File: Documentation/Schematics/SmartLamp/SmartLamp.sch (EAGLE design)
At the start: 25 parts, among them IC1 DS3231/SO, J1 POWER_JACKPTH_BREAD, Q1 IRF1404, Q2 IRF1404, Q3 IRF1404, U1 HM-10

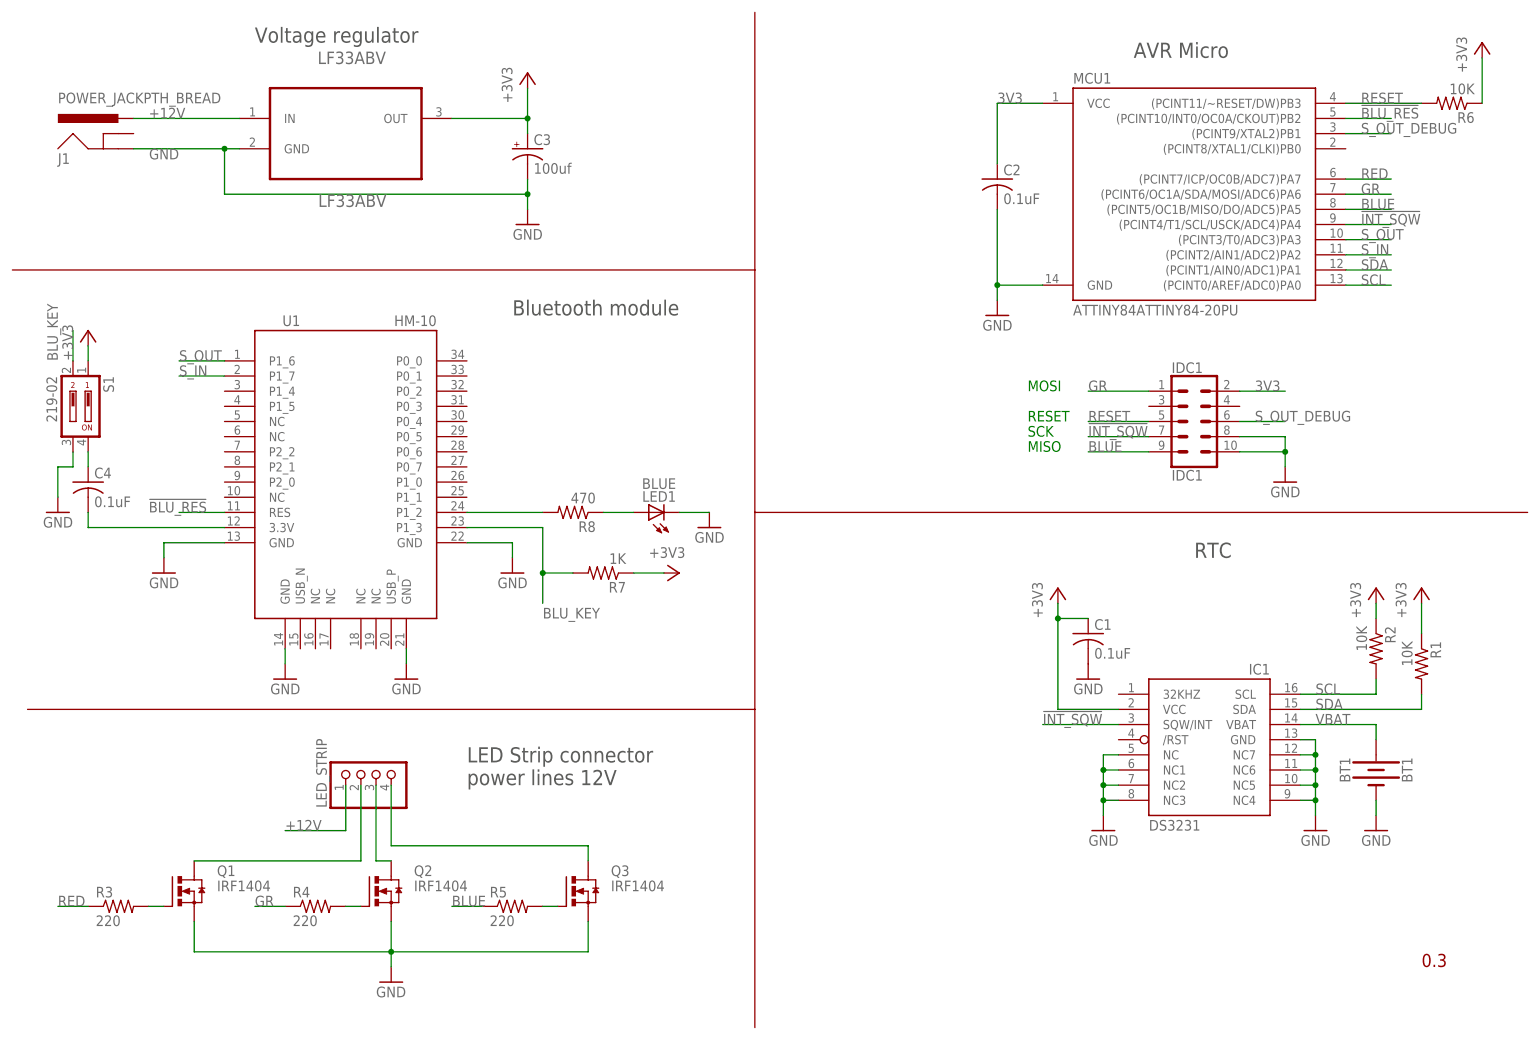
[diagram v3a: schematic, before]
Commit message: Replaced RTC device, battery holder and switch, parts to buy..
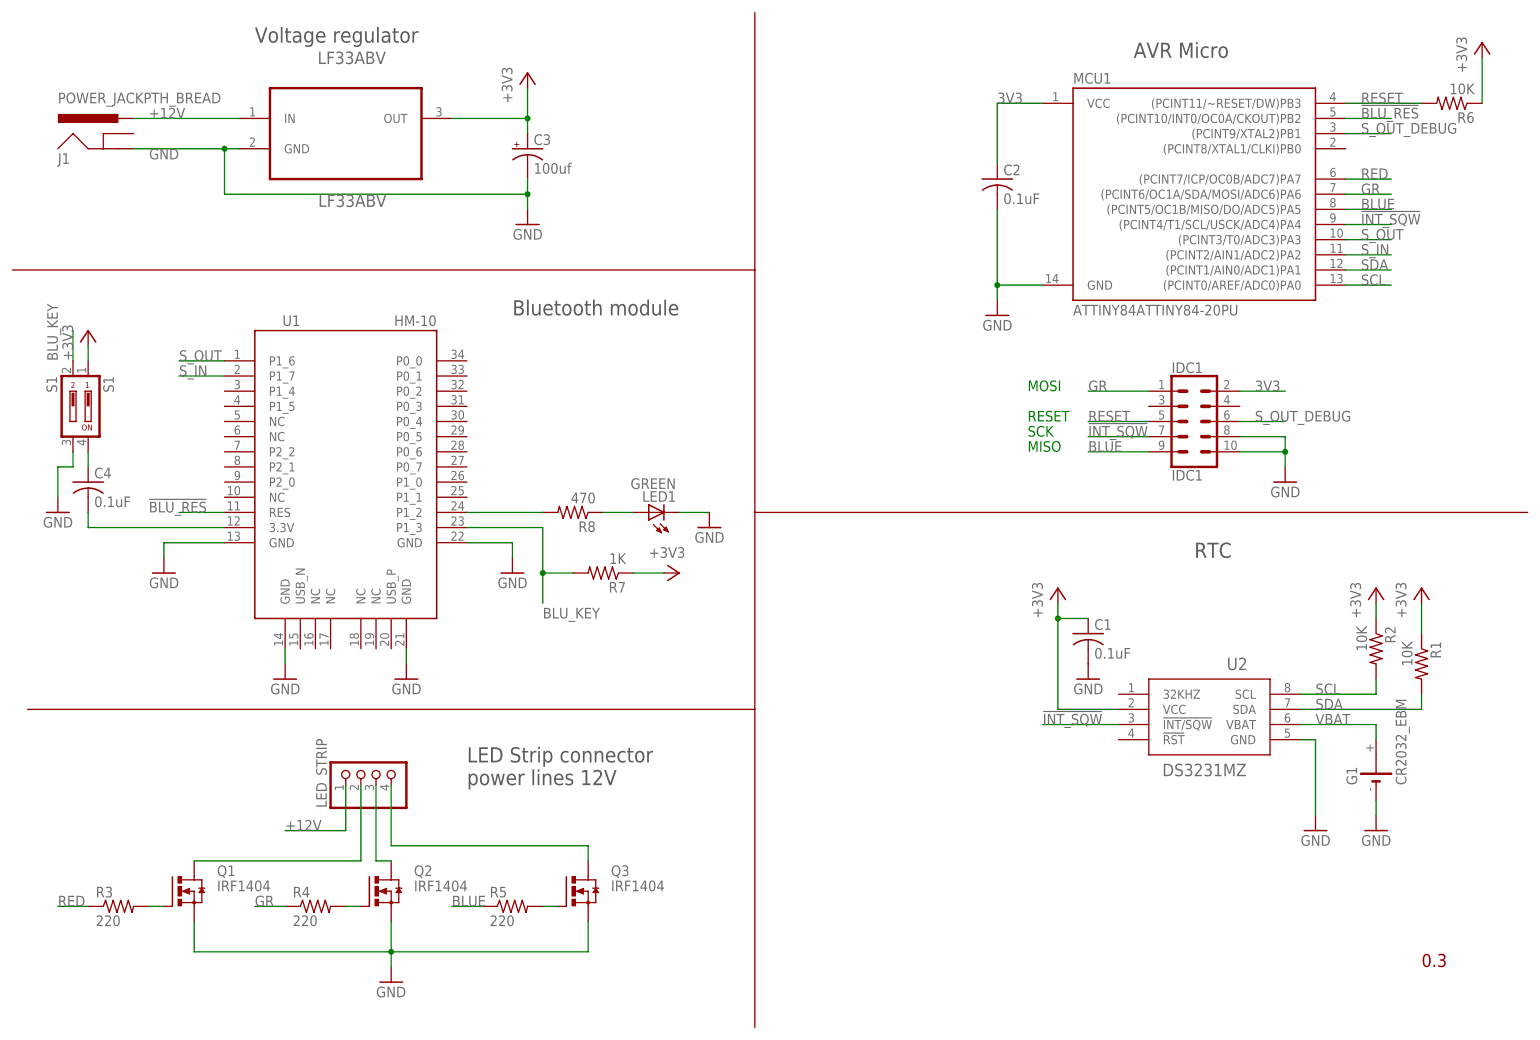
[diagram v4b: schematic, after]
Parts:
- removed BT1: BT1, SparkFun-Batteries:BATTERY-20MM_SMD_4LEGS
- removed IC1: DS3231/SO, adafruit:DS3231/SO
- added G1: CR2032_EBM, CuSTOM_GB:CR2032_EBM
- added U2: DS3231MZ, Maxim_RTC:DS3231MZ
- LED1: value BLUE -> GREEN
- S1: value 219-02 -> S1; device switch-dil:219-02 -> switch-dil:SD4-02
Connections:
- net !INT_SQW: now also U2.!INT/SQW; no longer IC1.SQW/INT
- net +3V3: now also U2.VCC; no longer IC1.VCC
- net GND: now also G1.-, U2.GND; no longer BT1.-, IC1.GND, IC1.NC, IC1.NC1, IC1.NC2, IC1.NC3, IC1.NC4, IC1.NC5, IC1.NC6, IC1.NC7
- net SCL: now also U2.SCL; no longer IC1.SCL
- net SDA: now also U2.SDA; no longer IC1.SDA
- net VBAT: now also G1.+, U2.VBAT; no longer BT1.+, IC1.VBAT

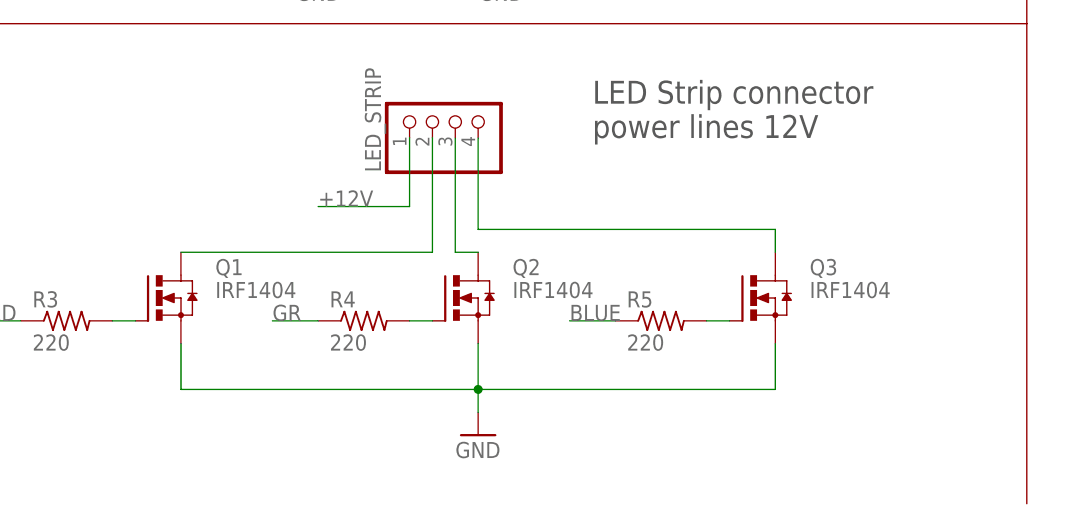
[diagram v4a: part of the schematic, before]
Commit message: Added datasheet for new mosfet IRLZ44n, small changes to HM-10 test program.
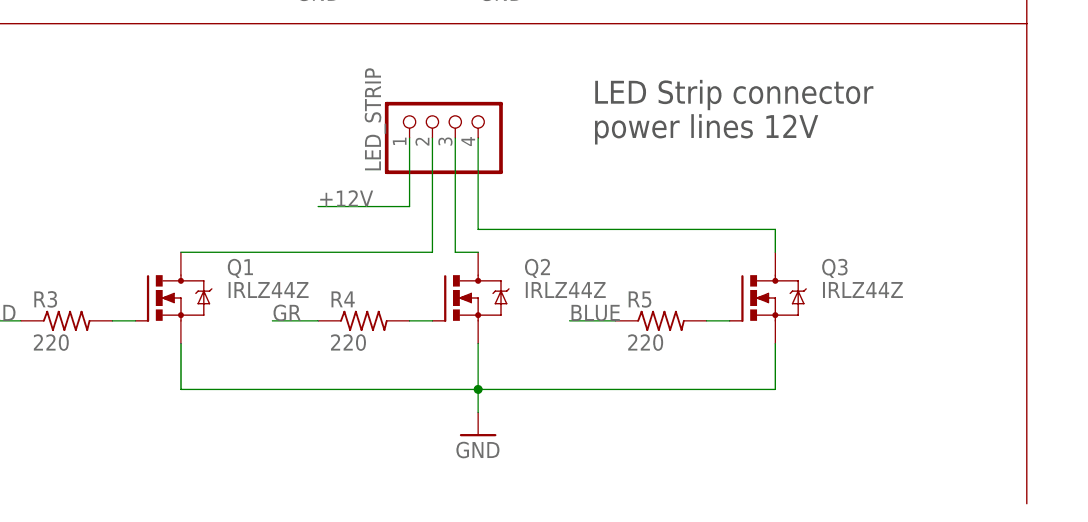
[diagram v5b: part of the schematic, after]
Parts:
- Q1, Q2, Q3: value IRF1404 -> IRLZ44Z; device transistor-power:IRFI540NPBF -> transistor-power:IRLZ44Z
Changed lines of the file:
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@@
 <part name="GND12" library="supply1" deviceset="GND" device=""/>
 <part name="C4" library="adafruit" deviceset="C-US" device="025-024X044" value="0.1uF"/>
-<part name="Q1" library="transistor-power" deviceset="IRFI540NPBF" device="" value="IRF1404"/>
-<part name="Q2" library="transistor-power" deviceset="IRFI540NPBF" device="" value="IRF1404"/>
-<part name="Q3" library="transistor-power" deviceset="IRFI540NPBF" device="" value="IRF1404"/>
 <part name="GND10" library="supply1" deviceset="GND" device=""/>
 <part name="LED_STRIP" library="pinhead" deviceset="PINHD-1X4" device=""/>
@@
 <part name="G1" library="CuSTOM_GB" deviceset="CR2032_EBM" device=""/>
 <part name="U2" library="Maxim_RTC" deviceset="DS3231MZ" device=""/>
+<part name="Q1" library="transistor-power" deviceset="IRLZ44Z" device=""/>
+<part name="Q2" library="transistor-power" deviceset="IRLZ44Z" device=""/>
+<part name="Q3" library="transistor-power" deviceset="IRLZ44Z" device=""/>
 </parts>
 <sheets>
@@
 <instance part="GND12" gate="1" x="119.38" y="88.9" rot="MR0"/>
 <instance part="C4" gate="G$1" x="15.24" y="96.52"/>
-<instance part="Q1" gate="G$1" x="30.48" y="27.94"/>
-<instance part="Q2" gate="G$1" x="63.5" y="27.94"/>
-<instance part="Q3" gate="G$1" x="96.52" y="27.94"/>
 <instance part="GND10" gate="1" x="66.04" y="12.7"/>
 <instance part="LED_STRIP" gate="A" x="63.5" y="48.26" rot="R90"/>
@@
 <instance part="G1" gate="G$1" x="231.14" y="48.26" rot="R90"/>
 <instance part="U2" gate="A" x="203.2" y="58.42"/>
+<instance part="Q1" gate="G$1" x="30.48" y="27.94"/>
+<instance part="Q2" gate="G$1" x="63.5" y="27.94"/>
+<instance part="Q3" gate="G$1" x="96.52" y="27.94"/>
 </instances>
 <busses>
@@
 </segment>
 <segment>
-<pinref part="Q1" gate="G$1" pin="S"/>
 <wire x1="33.02" y1="22.86" x2="33.02" y2="17.78" width="0.1524" layer="91"/>
-<pinref part="Q2" gate="G$1" pin="S"/>
 <wire x1="33.02" y1="17.78" x2="66.04" y2="17.78" width="0.1524" layer="91"/>
 <wire x1="66.04" y1="17.78" x2="66.04" y2="22.86" width="0.1524" layer="91"/>
-<pinref part="Q3" gate="G$1" pin="S"/>
 <wire x1="99.06" y1="22.86" x2="99.06" y2="17.78" width="0.1524" layer="91"/>
 <wire x1="99.06" y1="17.78" x2="66.04" y2="17.78" width="0.1524" layer="91"/>
@@
 <pinref part="GND10" gate="1" pin="GND"/>
 <wire x1="66.04" y1="15.24" x2="66.04" y2="17.78" width="0.1524" layer="91"/>
+<pinref part="Q1" gate="G$1" pin="S"/>
+<pinref part="Q2" gate="G$1" pin="S"/>
+<pinref part="Q3" gate="G$1" pin="S"/>
 </segment>
 <segment>
@@
 <net name="N$3" class="1">
 <segment>
-<pinref part="Q1" gate="G$1" pin="D"/>
 <wire x1="33.02" y1="33.02" x2="60.96" y2="33.02" width="0.1524" layer="91"/>
 <pinref part="LED_STRIP" gate="A" pin="2"/>
 <wire x1="60.96" y1="45.72" x2="60.96" y2="33.02" width="0.1524" layer="91"/>
+<pinref part="Q1" gate="G$1" pin="D"/>
 </segment>
 </net>
 <net name="N$4" class="1">
 <segment>
-<pinref part="Q2" gate="G$1" pin="D"/>
 <wire x1="63.5" y1="33.02" x2="66.04" y2="33.02" width="0.1524" layer="91"/>
 <pinref part="LED_STRIP" gate="A" pin="3"/>
 <wire x1="63.5" y1="33.02" x2="63.5" y2="45.72" width="0.1524" layer="91"/>
+<pinref part="Q2" gate="G$1" pin="D"/>
 </segment>
 </net>
 <net name="N$6" class="1">
 <segment>
-<pinref part="Q3" gate="G$1" pin="D"/>
 <wire x1="66.04" y1="35.56" x2="99.06" y2="35.56" width="0.1524" layer="91"/>
 <wire x1="99.06" y1="35.56" x2="99.06" y2="33.02" width="0.1524" layer="91"/>
 <pinref part="LED_STRIP" gate="A" pin="4"/>
 <wire x1="66.04" y1="45.72" x2="66.04" y2="35.56" width="0.1524" layer="91"/>
+<pinref part="Q3" gate="G$1" pin="D"/>
 </segment>
 </net>
 <net name="N$7" class="0">
 <segment>
-<pinref part="Q1" gate="G$1" pin="G"/>
 <pinref part="R3" gate="G$1" pin="2"/>
 <wire x1="27.94" y1="25.4" x2="25.4" y2="25.4" width="0.1524" layer="91"/>
+<pinref part="Q1" gate="G$1" pin="G"/>
 </segment>
 </net>
@@
 <segment>
 <pinref part="R4" gate="G$1" pin="2"/>
+<wire x1="58.42" y1="25.4" x2="60.96" y2="25.4" width="0.1524" layer="91"/>
 <pinref part="Q2" gate="G$1" pin="G"/>
-<wire x1="58.42" y1="25.4" x2="60.96" y2="25.4" width="0.1524" layer="91"/>
 </segment>
 </net>
@@
 <segment>
 <pinref part="R5" gate="G$1" pin="2"/>
+<wire x1="91.44" y1="25.4" x2="93.98" y2="25.4" width="0.1524" layer="91"/>
 <pinref part="Q3" gate="G$1" pin="G"/>
-<wire x1="91.44" y1="25.4" x2="93.98" y2="25.4" width="0.1524" layer="91"/>
-</segment>
-</net>
+</segment>
+</net>

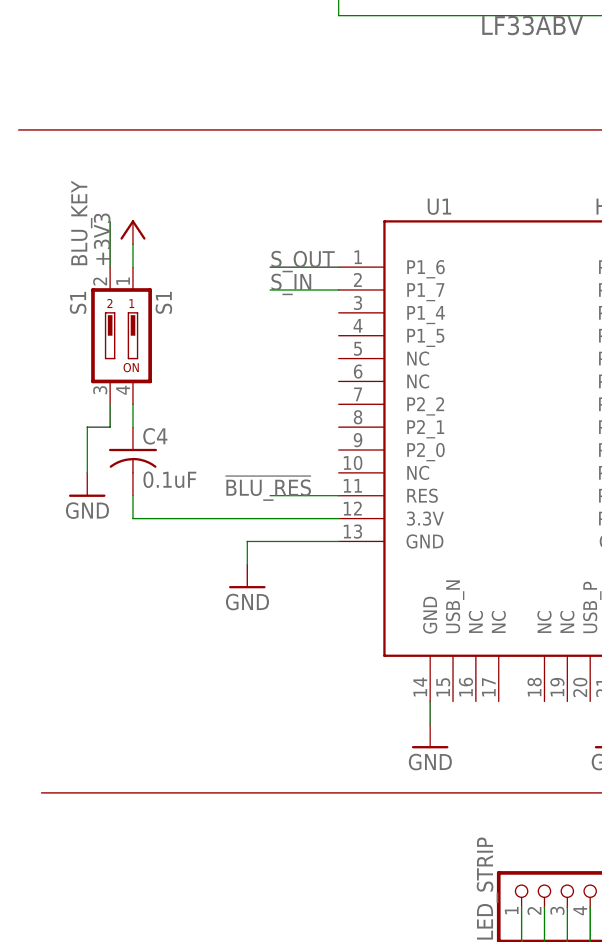
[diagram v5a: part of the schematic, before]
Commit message: Changed dip switch to cut GND instead of VCC to bluetooth module.
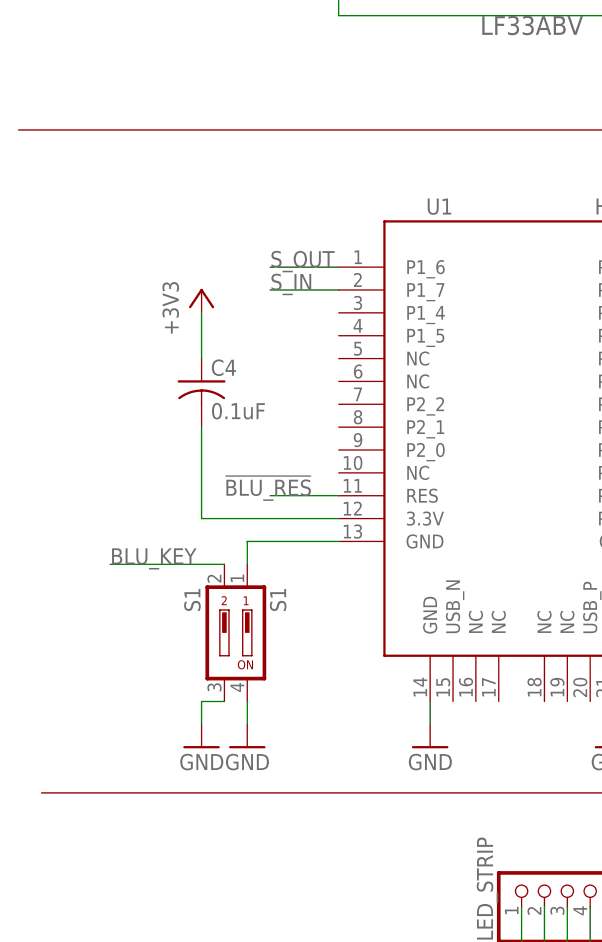
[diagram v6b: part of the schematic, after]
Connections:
- net +3V3: now also C4.1; no longer S1.1
- net GND: now also S1.4; no longer U1.GND@1
- net N$1: no longer C4.2
- net N$2: now also S1.1, U1.GND@1; no longer C4.1, S1.4
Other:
- moved on the sheet: C4, S1
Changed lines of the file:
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@@
 <instance part="R8" gate="G$1" x="96.52" y="91.44" rot="R180"/>
 <instance part="LED1" gate="G$1" x="109.22" y="91.44" rot="R90"/>
-<instance part="GND7" gate="1" x="27.94" y="81.28" rot="MR0"/>
+<instance part="GND7" gate="1" x="27.94" y="63.5" rot="MR0"/>
 <instance part="GND8" gate="1" x="48.26" y="63.5" rot="MR0"/>
 <instance part="GND9" gate="1" x="68.58" y="63.5" rot="MR0"/>
 <instance part="GND11" gate="1" x="86.36" y="81.28" rot="MR0"/>
 <instance part="GND12" gate="1" x="119.38" y="88.9" rot="MR0"/>
-<instance part="C4" gate="G$1" x="15.24" y="96.52"/>
+<instance part="C4" gate="G$1" x="22.86" y="104.14"/>
 <instance part="GND10" gate="1" x="66.04" y="12.7"/>
 <instance part="LED_STRIP" gate="A" x="63.5" y="48.26" rot="R90"/>
@@
 <instance part="FRAME1" gate="G$1" x="0" y="0"/>
 <instance part="GND13" gate="1" x="231.14" y="38.1" rot="MR0"/>
-<instance part="S1" gate="1" x="15.24" y="109.22" rot="R180"/>
+<instance part="S1" gate="1" x="27.94" y="76.2" rot="R180"/>
 <instance part="+3V1" gate="G$1" x="248.92" y="170.18"/>
 <instance part="+3V2" gate="G$1" x="177.8" y="78.74"/>
@@
 <instance part="+3V5" gate="G$1" x="88.9" y="165.1"/>
 <instance part="+3V6" gate="G$1" x="114.3" y="81.28" rot="R270"/>
-<instance part="+3V7" gate="G$1" x="15.24" y="121.92"/>
+<instance part="+3V7" gate="G$1" x="22.86" y="114.3"/>
 <instance part="GND5" gate="1" x="167.64" y="124.46" rot="MR0"/>
-<instance part="GND6" gate="1" x="10.16" y="91.44" rot="MR0"/>
+<instance part="GND6" gate="1" x="22.86" y="63.5" rot="MR0"/>
 <instance part="G1" gate="G$1" x="231.14" y="48.26" rot="R90"/>
 <instance part="U2" gate="A" x="203.2" y="58.42"/>
@@
 </segment>
 <segment>
-<wire x1="27.94" y1="86.36" x2="27.94" y2="83.82" width="0.1524" layer="91"/>
-<pinref part="GND7" gate="1" pin="GND"/>
-<pinref part="U1" gate="G$1" pin="GND@1"/>
-<wire x1="27.94" y1="86.36" x2="38.1" y2="86.36" width="0.1524" layer="91"/>
-</segment>
-<segment>
 <pinref part="U1" gate="G$1" pin="GND@2"/>
 <wire x1="48.26" y1="68.58" x2="48.26" y2="66.04" width="0.1524" layer="91"/>
@@
 <segment>
 <pinref part="S1" gate="1" pin="3"/>
-<wire x1="12.7" y1="101.6" x2="12.7" y2="99.06" width="0.1524" layer="91"/>
-<wire x1="12.7" y1="99.06" x2="10.16" y2="99.06" width="0.1524" layer="91"/>
-<wire x1="10.16" y1="99.06" x2="10.16" y2="93.98" width="0.1524" layer="91"/>
+<wire x1="25.4" y1="68.58" x2="22.86" y2="68.58" width="0.1524" layer="91"/>
+<wire x1="22.86" y1="68.58" x2="22.86" y2="66.04" width="0.1524" layer="91"/>
 <pinref part="GND6" gate="1" pin="GND"/>
+</segment>
+<segment>
+<pinref part="S1" gate="1" pin="4"/>
+<pinref part="GND7" gate="1" pin="GND"/>
+<wire x1="27.94" y1="68.58" x2="27.94" y2="66.04" width="0.1524" layer="91"/>
 </segment>
 </net>
@@
 <segment>
 <pinref part="S1" gate="1" pin="2"/>
-<wire x1="12.7" y1="116.84" x2="12.7" y2="121.92" width="0.1524" layer="91"/>
-<label x="10.16" y="116.84" size="1.778" layer="95" font="vector" rot="R90"/>
+<wire x1="25.4" y1="83.82" x2="12.7" y2="83.82" width="0.1524" layer="91"/>
+<label x="12.7" y="83.82" size="1.778" layer="95" font="vector"/>
 </segment>
 </net>
@@
 <segment>
 <pinref part="U1" gate="G$1" pin="3.3V"/>
-<wire x1="38.1" y1="88.9" x2="15.24" y2="88.9" width="0.1524" layer="91"/>
-<pinref part="C4" gate="G$1" pin="2"/>
-<wire x1="15.24" y1="91.44" x2="15.24" y2="88.9" width="0.1524" layer="91"/>
-</segment>
-</net>
-<net name="N$2" class="0">
-<segment>
-<pinref part="S1" gate="1" pin="4"/>
-<pinref part="C4" gate="G$1" pin="1"/>
-<wire x1="15.24" y1="101.6" x2="15.24" y2="99.06" width="0.1524" layer="91"/>
+<wire x1="38.1" y1="88.9" x2="22.86" y2="88.9" width="0.1524" layer="91"/>
+<wire x1="22.86" y1="88.9" x2="22.86" y2="99.06" width="0.1524" layer="91"/>
 </segment>
 </net>
@@
 </segment>
 <segment>
+<pinref part="C4" gate="G$1" pin="1"/>
+<pinref part="+3V7" gate="G$1" pin="+3V3"/>
+<wire x1="22.86" y1="106.68" x2="22.86" y2="111.76" width="0.1524" layer="91"/>
+</segment>
+</net>
+<net name="N$2" class="0">
+<segment>
+<pinref part="U1" gate="G$1" pin="GND@1"/>
+<wire x1="27.94" y1="86.36" x2="38.1" y2="86.36" width="0.1524" layer="91"/>
 <pinref part="S1" gate="1" pin="1"/>
-<wire x1="15.24" y1="119.38" x2="15.24" y2="116.84" width="0.1524" layer="91"/>
-<pinref part="+3V7" gate="G$1" pin="+3V3"/>
-</segment>
-</net>
+<wire x1="27.94" y1="86.36" x2="27.94" y2="83.82" width="0.1524" layer="91"/>
+</segment>
+</net>
